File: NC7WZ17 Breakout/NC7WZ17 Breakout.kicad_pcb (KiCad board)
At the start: 2 copper layers, 10.2 x 11.2 mm, 5 parts, among them J1 Conn_01x03, J2 Conn_01x04, U1 NC7WZ17P6X

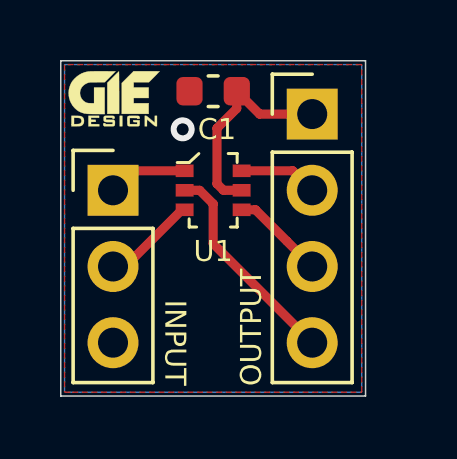
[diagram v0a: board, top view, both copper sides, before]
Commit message: Change header to header spacing to 0.3", Update header and IC silkscreen
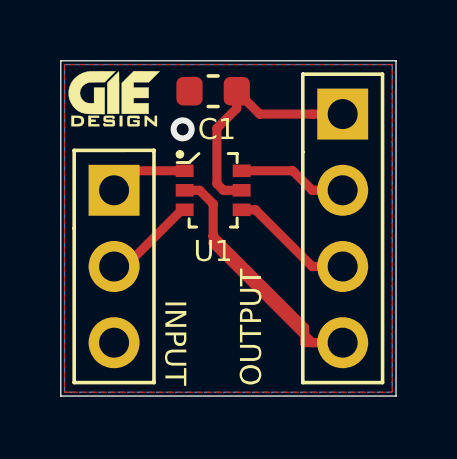
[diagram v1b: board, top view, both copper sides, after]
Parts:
- moved J2 1.02 mm to (112.5, 88.9)
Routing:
- net GND: track 7.13 -> 13.2 mm
- net VCC: track 7.10 -> 8.12 mm
- net /OUT2: track 3.13 -> 4.15 mm
- net /OUT1: track 2.62 -> 3.64 mm
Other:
- board size 10.2 x 11.2 mm -> 11.2 x 11.2 mm
- board text added: "OUT1 IN"
- board text added: "OUT2 IN"
- board text added: "VCC"
- board text removed: "IN1 OUT"
- board text removed: "IN2 OUT"
